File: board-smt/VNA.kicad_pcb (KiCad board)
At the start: 2 copper layers, 100 x 85 mm, 170 parts, among them J1 Conn_02x07_Odd_Even, J10 Conn_01x04, J11 Conn_01x01, J13 Barrel_Jack, J14 Conn_01x01, J15 Conn_01x02, J16 Conn_01x01, J18 Conn_01x01, J19 Conn_01x01, J2 Conn_Coaxial, J20 Conn_01x01, J21 Conn_01x01, J24 USB_B, J4 Conn_01x01, J5 Conn_01x01, J6 Conn_01x01, J7 Conn_01x01, J8 Conn_01x01, J9 Conn_Coaxial, Q3 S9018, SW1 SW_DPDT_x2, U1 SI5351A, U10 MT3608, U11 CN3052, U12 SI5351A, U13 MicroSD_SPI_CD, U2 LM339, U3 SA612, U4 SA612, U5 SA612, U6 LM358, U7 LM358, U8 AMS1117-3V3, U9 78M05_TO252, Y1 27 MHz

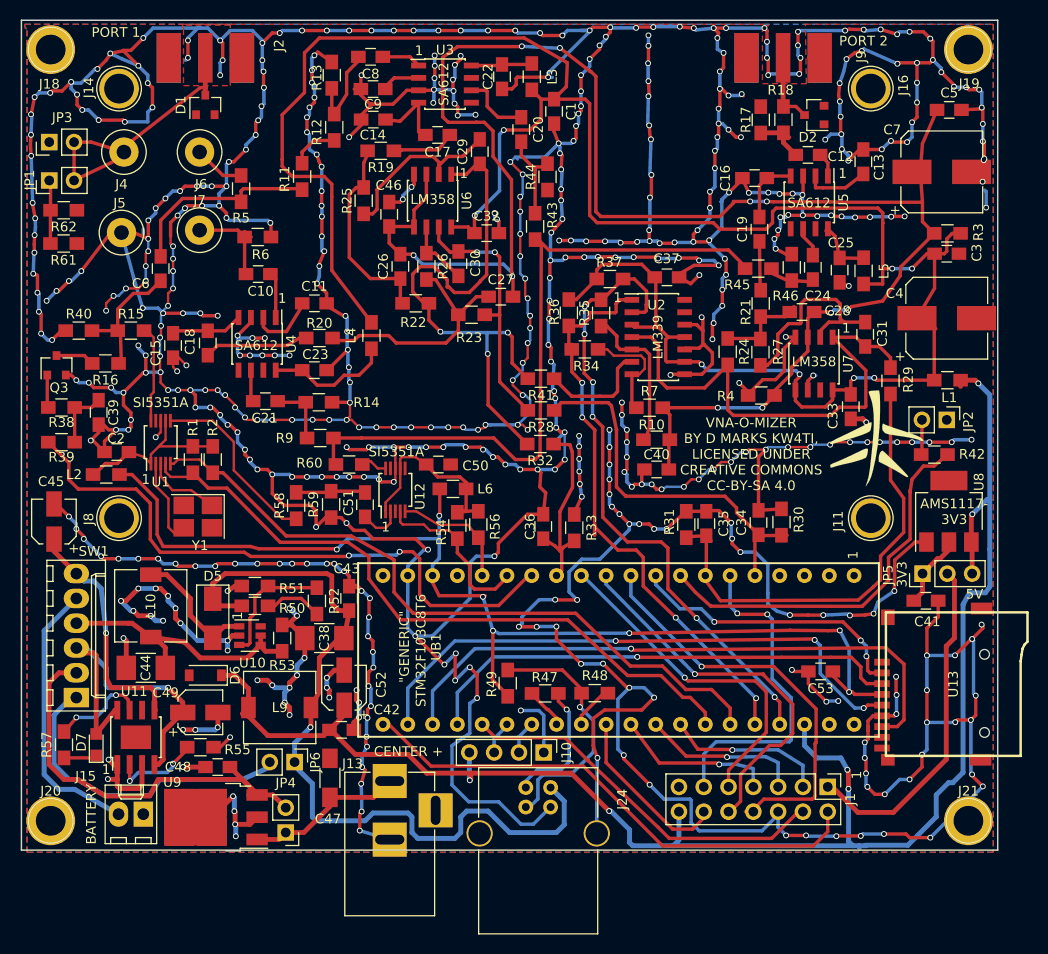
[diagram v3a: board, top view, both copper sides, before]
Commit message: Finally removed the bluepill!
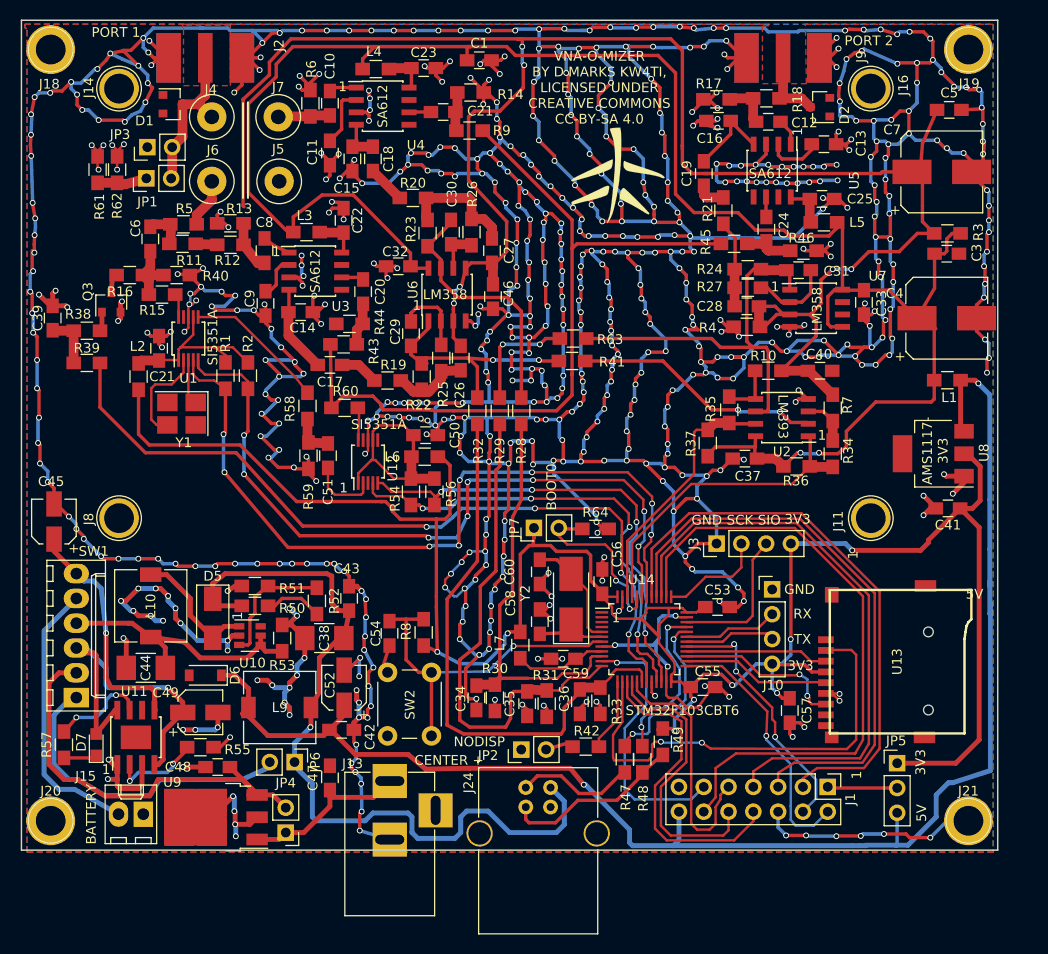
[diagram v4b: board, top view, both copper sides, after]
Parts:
- removed UB1: BLUEPILL, VNA:BLUEPILL
- added C54: 100 nF, Capacitors_SMD:C_0805_HandSoldering, F.Cu at (87.7, 112.8)
- added C55: 100 nF, Capacitors_SMD:C_0805_HandSoldering, F.Cu at (119.8, 118.3)
- added C56: 100 nF, Capacitors_SMD:C_0805_HandSoldering, F.Cu at (109.5, 107.5)
- added C57: 100 nF, Capacitors_SMD:C_0805_HandSoldering, F.Cu at (128.7, 120.7)
- added C58: 22 pF, Capacitors_SMD:C_0805_HandSoldering, F.Cu at (103.1, 111.6)
- added C59: 100 nF, Capacitors_SMD:C_0805_HandSoldering, F.Cu at (105.5, 115.4)
- added C60: 22 pF, Capacitors_SMD:C_0805_HandSoldering, F.Cu at (103.1, 106.5)
- added J3: Conn_01x04, Pin_Headers:Pin_Header_Straight_1x04_Pitch2.54mm, F.Cu at (121.2, 103.6)
- added JP7: Jumper_NC_Small, Pin_Headers:Pin_Header_Straight_1x02_Pitch2.54mm, F.Cu at (102.5, 102.0)
- added L7: Ferrite_Bead_Small, Inductors_SMD:L_0805_HandSoldering, F.Cu at (101.1, 114.0)
- added R63: 0R, Resistors_SMD:R_0805_HandSoldering, F.Cu at (106.5, 82.6)
- added R64: 10k, Resistors_SMD:R_0805_HandSoldering, F.Cu at (108.8, 102.1)
- added R8: 1k5, Resistors_SMD:R_0805_HandSoldering, F.Cu at (91.2, 112.7)
- added SW2: SW_DIP_x01, Buttons_Switches_THT:SW_PUSH_6mm, F.Cu at (87.5, 123.3)
- added U14: STM32F103C8T6, Housings_QFP:LQFP-48_7x7mm_Pitch0.5mm, F.Cu at (113.8, 113.4)
- added Y2: 8 MHz, Crystals:Crystal_SMD_5032-2pin_5.0x3.2mm_HandSoldering, F.Cu at (106.3, 109.3)
- C47: value 330 nF -> 1 uF; footprint Capacitors_SMD:C_1206_HandSoldering -> Capacitors_SMD:C_0805_HandSoldering
- Q3: value S9018 -> 2SC3356
- R41: value 1k -> 0R
- R49: value NC -> 1k5
- U2: value LM339 -> LM393; footprint Housings_SOIC:SOIC-14_3.9x8.7mm_Pitch1.27mm -> Housings_SOIC:SOIC-8_3.9x4.9mm_Pitch1.27mm
- Y1: value 27 MHz -> 25 MHz
- moved JP2 55.1 mm to (101.2, 124.7), turned to 90 degrees
- moved R42 46.6 mm to (107.8, 124.4)
- moved R29 40.1 mm to (99.0, 90.0)
- moved G*** 37.8 mm to (111.1, 65.9)
- moved R14 35.3 mm to (96.0, 57.4)
- moved R9 35.0 mm to (95.9, 61.3)
- moved C21 34.8 mm to (93.2, 59.4)
- moved R30 34.4 mm to (98.5, 119.4), turned to 90 degrees
- moved C34 34.0 mm to (96.6, 119.4), turned to 270 degrees
- moved C23 32.9 mm to (91.2, 54.9)
- moved J10 28.7 mm to (126.9, 108.3), turned to 0 degrees
- moved R36 28.1 mm to (129.4, 95.7), turned to 180 degrees
- moved L3 28.0 mm to (79.2, 71.7), turned to 180 degrees
- moved R34 27.5 mm to (133.1, 94.4), turned to 270 degrees
- moved U4 27.5 mm to (87.0, 58.8), turned to 0 degrees
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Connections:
- net DEMODCUR renamed PA0DEMODCUR
- net DEMODCUR2 renamed PA2DEMODCUR2
- net DEMODVOLT renamed PB0DEMODVOLT
- net SCL renamed PB6SCL
- net SCL2 renamed PB10SCL2
- net SDA renamed PB7SDA
- net SDA2 renamed PB11SDA2
- net SYNCSAMPLE renamed PB8SYNCSAMPLE
- C41 pad 1: Net-(C41-Pad1) -> +3V3
- J1 pad 10: MISO1 -> PA6MISO1
- J1 pad 8: SCK1 -> PA5SCK1
- J1 pad 9: MOSI1 -> PA7MOSI1
- J10 pad 2: Net-(J10-Pad2) -> PA10RX1
- J10 pad 3: Net-(J10-Pad3) -> PA9TX1
- J10 pad 4: +5V -> +3V3
- JP5 pad 1: Net-(C41-Pad1) -> +3V3
- R29 pad 2: Net-(C31-Pad1) -> Net-(R29-Pad2)
- R35 pad 2: SYNCSAMPLE2 -> PB9SYNCSAMPLE2
- R37 pad 1: SYNCSAMPLE2 -> PB9SYNCSAMPLE2
- R39 pad 2: ATTEN -> PB1ATTEN
- R42 pad 2: NODISPLAY -> PA3NODISPLAY
- R47 pad 1: Net-(R47-Pad1) -> Net-(J24-Pad2)
- R47 pad 2: Net-(J24-Pad2) -> PA11USBM
- R48 pad 1: Net-(R48-Pad1) -> Net-(J24-Pad3)
- R48 pad 2: Net-(J24-Pad3) -> PA12USBP
- R49 pad 1: +3V3 -> Net-(J24-Pad3)
- R49 pad 2: Net-(J24-Pad3) -> +3V3
- U13 pad 2: SD_CS -> PA4SD_CS
- U13 pad 3: Net-(U13-Pad3) -> PB15MOSI2
- U13 pad 5: Net-(U13-Pad5) -> PB13SCK2
- U13 pad 7: Net-(U13-Pad7) -> PB14MISO2
- U2 pad 2: SYNCSAMPLE2 -> Net-(R41-Pad1)
- U2 pad 3: FILT5V -> Net-(R34-Pad1)
- U2 pad 4: Net-(C31-Pad1) -> GND
- U2 pad 6: Net-(R41-Pad1) -> Net-(C31-Pad1)
- U2 pad 7: Net-(R34-Pad1) -> PB9SYNCSAMPLE2
- U2 pad 8: GND -> FILT5V
- U8 pad 2: Net-(C41-Pad1) -> +3V3
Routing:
- net +3V3: track 116.5 -> 228.8 mm, vias 7 -> 8
- net PB1ATTEN: track 0.00 -> 82.9 mm, vias 0 -> 4
- net SYNCSAMPLE2: track 64.8 -> 0.00 mm, vias 6 -> 0
- net GND: track 1396.7 -> 1461.3 mm, vias 555 -> 646
- net ATTEN: track 63.5 -> 0.00 mm, vias 2 -> 0
- net Net-(U13-Pad7): track 62.7 -> 0.00 mm, vias 1 -> 0
- net Net-(U13-Pad5): track 59.3 -> 0.00 mm, vias 3 -> 0
- net Net-(U13-Pad3): track 50.1 -> 0.00 mm, vias 1 -> 0
- net PA4SD_CS: track 0.00 -> 47.8 mm, vias 0 -> 2
- net PA15: track 18.2 -> 65.3 mm
- net PB3: track 16.3 -> 59.8 mm, vias 1 -> 0
- net PB4: track 16.7 -> 59.5 mm, vias 1 -> 0
- net SCK1: track 42.8 -> 0.00 mm, vias 1 -> 0
- net PB5: track 17.1 -> 59.6 mm, vias 1 -> 0
- net NODISPLAY: track 40.0 -> 0.00 mm
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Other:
- board text added: "BOOT0"
- board text added: "GND"
- board text added: "LM393"
- board text added: "NODISP"
- board text added: "RX"
- board text added: "SCK"
- board text added: "SIO"
- board text added: "STM32F103CBT6"
- board text added: "TX"
- board text removed: "LM339"

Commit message: Choke bridge
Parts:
- removed G***: LOGO, VNA:VNAOMizer
- removed JP4, JP6: Jumper_NC_Small, Pin_Headers:Pin_Header_Straight_1x02_Pitch2.54mm
- added D3: SS14, Diodes_SMD:D_SMA, F.Cu at (76.5, 126.0)
- added D4: SS14, Diodes_SMD:D_SMA, F.Cu at (78.4, 131.1)
- added R65: NC, Resistors_SMD:R_0805_HandSoldering, F.Cu at (64.9, 59.8)
- added R66: NC, Resistors_SMD:R_0805_HandSoldering, F.Cu at (70.7, 74.6)
- added R67: NC, Resistors_SMD:R_0805_HandSoldering, F.Cu at (63.7, 67.8)
- D6: footprint Diodes_SMD:D_SOD-123 -> Diodes_SMD:D_MiniMELF
- R30, R31, R33: value 1k5 -> 2k2
- R50: value 1k -> 0R
- R51: value 270R -> 220R
- R52: value 1k -> 1k5
- moved R13 6.55 mm to (72.8, 77.2), turned to 270 degrees
- moved R40 4.81 mm to (64.2, 71.6), turned to 270 degrees
- moved JP1 4.63 mm to (58.3, 65.1), turned to 180 degrees
- moved R62 4.20 mm to (55.7, 64.4)
- moved R61 4.10 mm to (53.8, 64.4)
- moved D1 3.91 mm to (65.2, 62.5), turned to 90 degrees
- moved R12 3.14 mm to (74.1, 71.4)
- moved R11 3.09 mm to (69.2, 71.4)
- moved C6 2.81 mm to (66.0, 72.6)
- moved R5 2.80 mm to (66.6, 68.1), turned to 270 degrees
- moved JP3 2.47 mm to (61.6, 65.1), turned to 180 degrees
- moved R16 2.02 mm to (62.8, 75.0)
- moved R15 1.84 mm to (66.0, 77.2), turned to 270 degrees
- moved C8 0.85 mm to (74.1, 73.9), turned to 180 degrees
- moved SW1 0.74 mm to (54.9, 119.5)
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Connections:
- J24 pad 1: POWFILT -> USBPWR
- SW1 pad 1: Net-(JP6-Pad2) -> POWFILT
- SW1 pad 2: REG5VOUT -> Net-(D3-Pad1)
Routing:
- net GND: track 1461.3 -> 1517.7 mm, vias 646 -> 666
- net Net-(D3-Pad1): track 0.00 -> 47.5 mm
- net 2V0: track 196.3 -> 152.4 mm
- net USBPWR: track 0.00 -> 37.9 mm
- net REG5VOUT: track 44.1 -> 10.3 mm
- net Net-(JP6-Pad2): track 33.0 -> 0.00 mm
- net POWFILT: track 84.1 -> 71.1 mm, vias 1 -> 0
- net +5V: track 154.5 -> 150.5 mm
- net PA1: track 28.0 -> 31.5 mm
- net Net-(D1-Pad3): track 17.3 -> 20.7 mm
- net Net-(R11-Pad1): track 2.20 -> 4.32 mm
- net Net-(Q3-Pad3): track 1.99 -> 3.83 mm
- net Net-(C49-Pad1): track 36.4 -> 37.9 mm
- net Net-(C6-Pad1): track 7.25 -> 8.80 mm
- net Net-(J24-Pad2): track 12.9 -> 11.4 mm
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
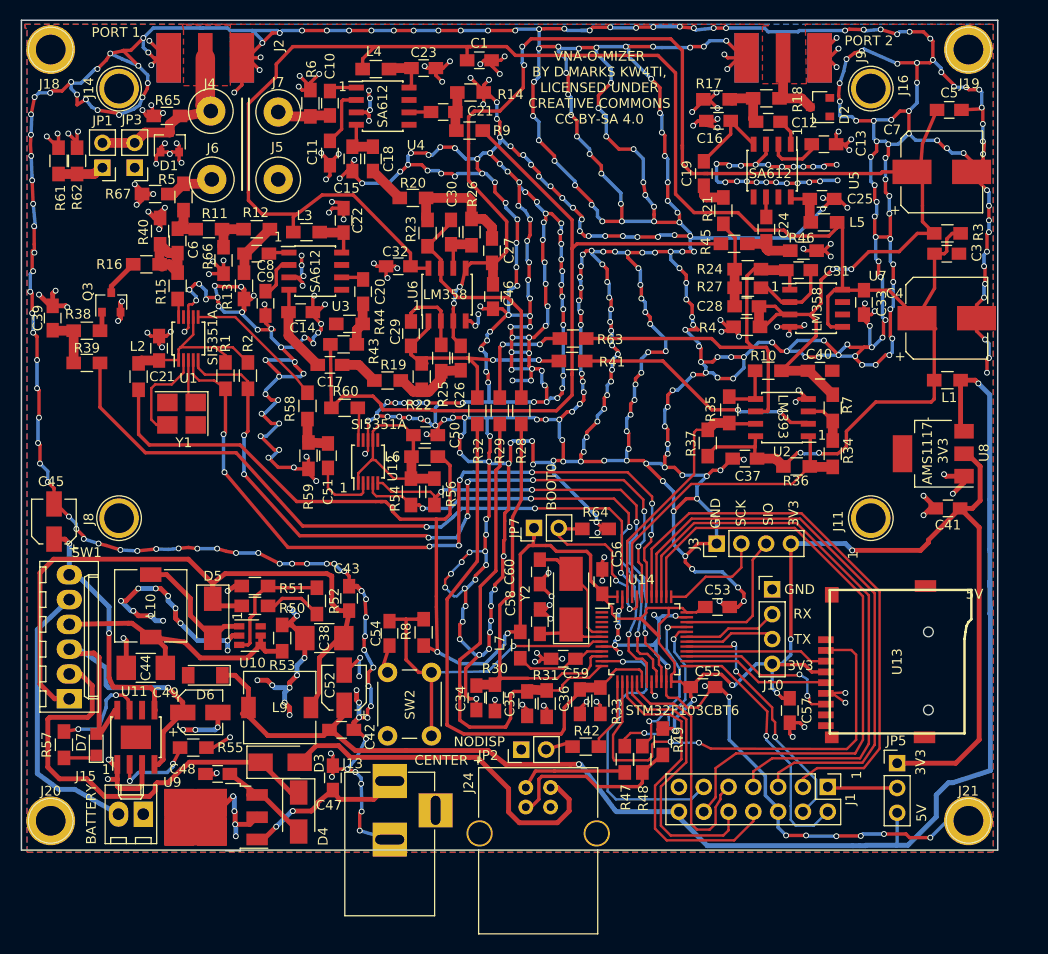
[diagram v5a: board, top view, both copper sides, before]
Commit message: Changed to resistive bridge
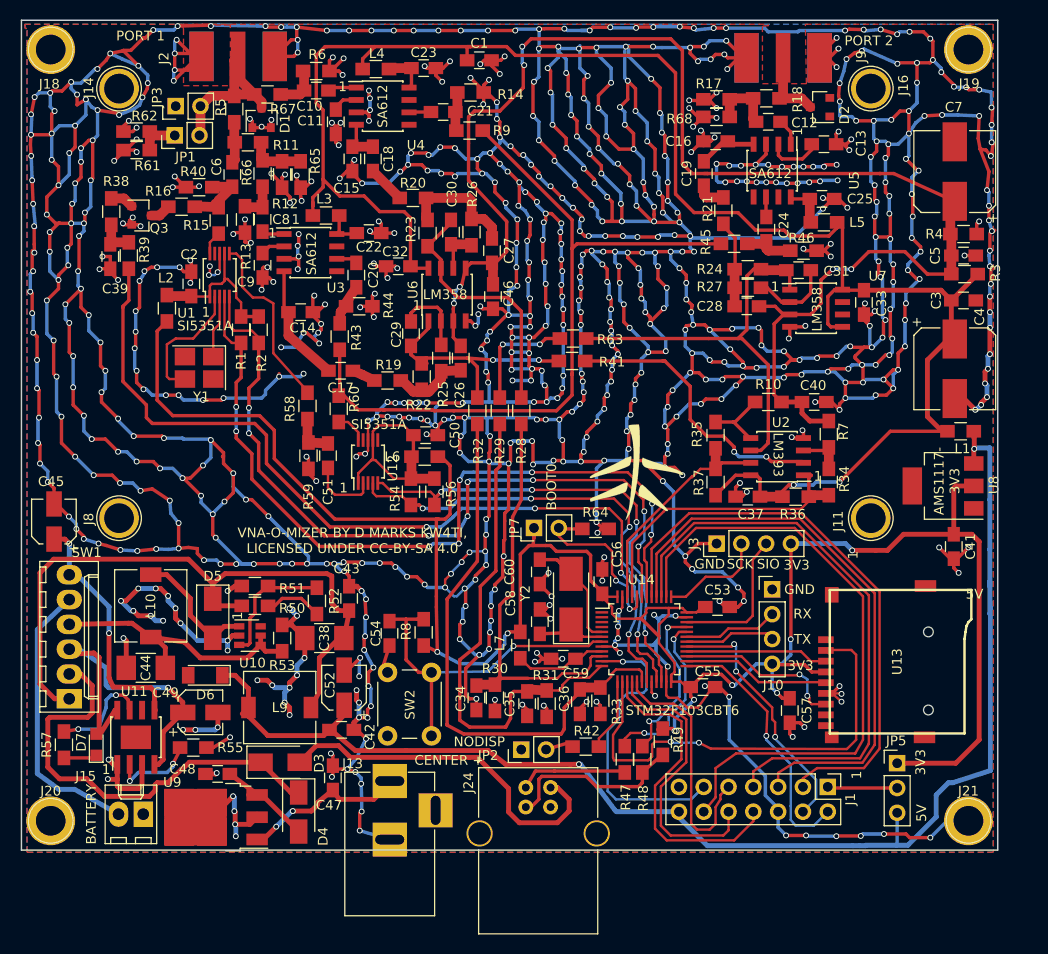
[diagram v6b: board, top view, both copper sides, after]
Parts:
- removed J4, J5, J6, J7: Conn_01x01, Connectors:1pin
- added G***: LOGO, VNA:VNAOMizer, F.Cu at (113.0, 96.3)
- added R68: 22R, Resistors_SMD:R_0805_HandSoldering, F.Cu at (121.2, 59.9)
- R11, R5: value 220R -> 47R
- R12: value 51R -> 100R
- R13, R6: value 5R1 -> 4R7
- R65: value NC -> 100R
- R66, R67: value NC -> 120R
- moved R4 24.1 mm to (146.5, 71.9), turned to 0 degrees
- moved R67 15.4 mm to (75.2, 57.6), turned to 0 degrees
- moved C5 15.0 mm to (146.5, 74.1)
- moved R65 15.0 mm to (78.6, 65.8), turned to 90 degrees
- moved R38 12.5 mm to (59.2, 69.6), turned to 270 degrees
- moved R39 11.8 mm to (61.0, 74.1), turned to 270 degrees
- moved R5 10.4 mm to (71.8, 59.1)
- moved R11 9.76 mm to (73.2, 62.5)
- moved R66 9.76 mm to (74.7, 65.7)
- moved D1 9.73 mm to (74.6, 60.0)
- moved Q3 9.42 mm to (62.3, 70.0), turned to 0 degrees
- moved C6 8.81 mm to (71.6, 65.8)
- moved C39 8.63 mm to (59.1, 74.2), turned to 270 degrees
- moved JP1 8.10 mm to (65.7, 61.8), turned to 90 degrees
- moved R61 8.08 mm to (61.8, 63.3), turned to 0 degrees
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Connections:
- C10 pad 2: SAMPCUR -> SAMPPORT
- R12 pad 1: SAMPVOLT -> GND
- R5 pad 1: Net-(J6-Pad1) -> Net-(D1-Pad3)
- R6 pad 1: SAMPCUR -> SAMPPORT
- R65 pad 1: Net-(D1-Pad3) -> GND
- R65 pad 2: GND -> Net-(R11-Pad1)
- R66 pad 2: GND -> SAMPVOLT
- R67 pad 1: Net-(J6-Pad1) -> Net-(D1-Pad3)
- R67 pad 2: GND -> SAMPPORT
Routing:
- net GND: track 1517.7 -> 1891.0 mm, vias 666 -> 797
- net FILT5V: track 196.8 -> 185.3 mm
- net +5V: track 150.5 -> 141.0 mm
- net PB1ATTEN: track 82.9 -> 91.3 mm
- net Net-(J6-Pad1): track 6.53 -> 0.00 mm
- net SAMPCUR: track 5.96 -> 0.00 mm
- net SAMPPORT: track 0.00 -> 4.61 mm
- net Net-(R58-Pad1): track 14.5 -> 18.7 mm
- net Net-(C11-Pad1): track 6.10 -> 2.65 mm
- net Net-(R41-Pad1): track 25.5 -> 29.0 mm
- net PB7SDA: track 76.0 -> 79.4 mm
- net PB6SCL: track 80.5 -> 83.9 mm
- net Net-(C14-Pad2): track 8.96 -> 12.3 mm
- net Net-(U1-Pad2): track 10.3 -> 13.5 mm
- net Net-(R43-Pad2): track 79.9 -> 76.9 mm
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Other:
- board text added: "VNA-O-MIZER BY D MARKS KW4TI, LICENSED UNDER CC-BY-SA 4.0"
- board text removed: "VNA-O-MIZER BY D MARKS KW4TI, LICENSED UNDER CREATIVE COMMONS CC-BY-SA 4.0"
